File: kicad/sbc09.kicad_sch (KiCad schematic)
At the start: 78 parts, among them J1 Conn_01x04_Male, J2 Conn_01x06_Male, J3 Conn_01x06_Male, J4 Conn_01x06_Male, J5 Conn_02x05_Odd_Even, J6 Conn_02x25_Odd_Even, J7 Conn_02x05_Odd_Even, Q1 2N7000, SW1 SW_Push, U1 74HCT245, U10 SST39SF040-DIP, U11 XR68C681CJ, U12 MAX232, U2 74HCT245, U3 74HCT245, U4 MC6809E, U5 74HCT32, U6 EPM7128SLC84, U7 71256SA15TPG, U8 AS6C4008-55PCN, U9 SST39SF040-DIP, X1 8MHz, X2 3.6864MHz

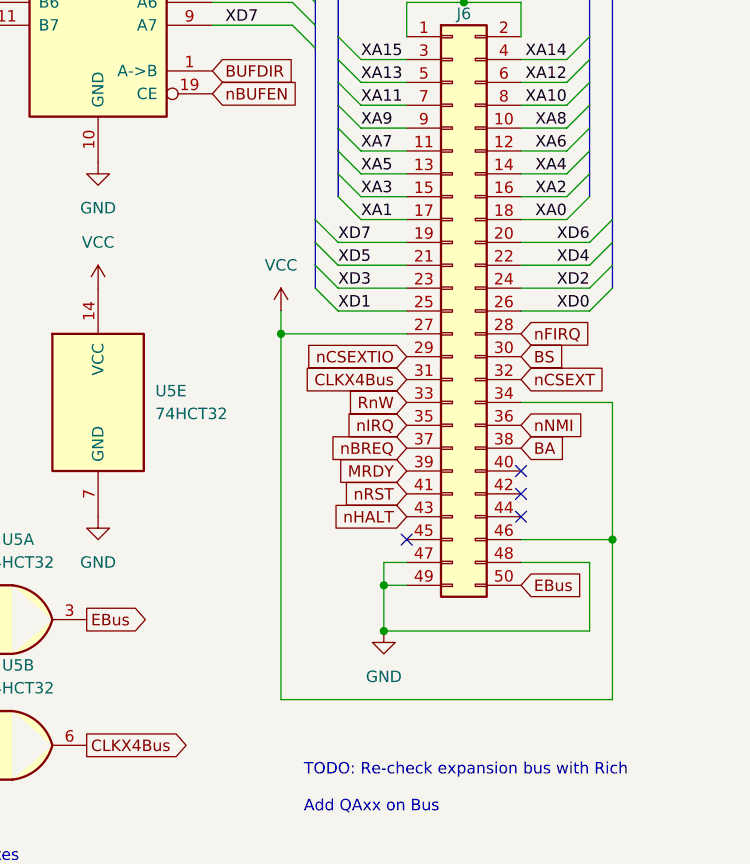
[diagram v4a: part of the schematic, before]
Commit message: KiCAD: Split VCC/VCCBUS and redraw planes
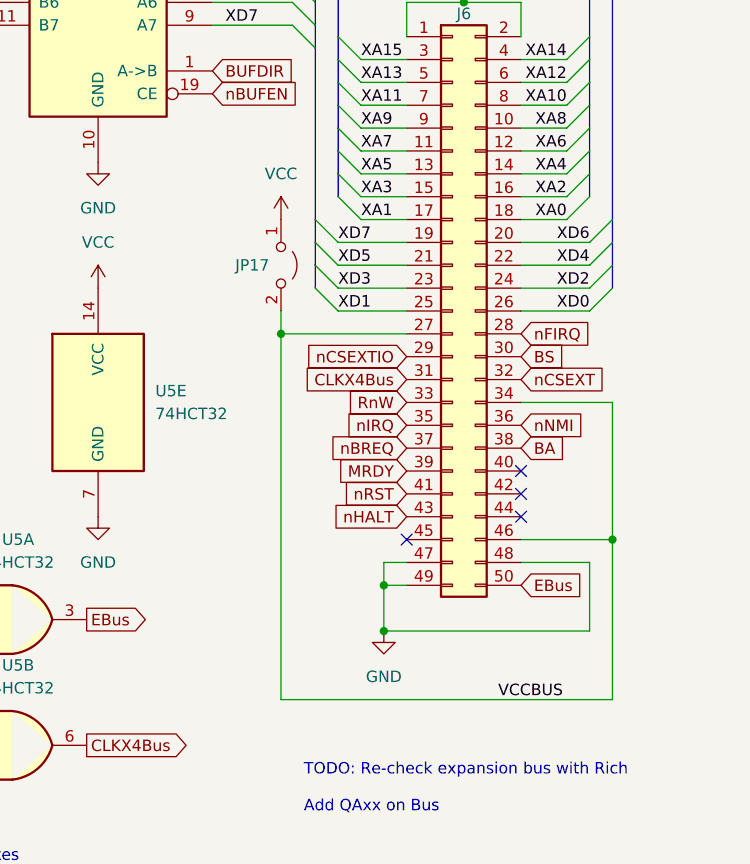
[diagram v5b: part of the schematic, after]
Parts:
- added JP17: Jumper_2_Open, Connector_PinHeader_2.54mm:PinHeader_1x02_P2.54mm_Vertical, symbol Jumper:Jumper_2_Open
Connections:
- net VCC: now also JP17.1 (A); no longer J6.27 (Pin_27), J6.34 (Pin_34), J6.46 (Pin_46)
- new net VCCBUS: J6.27 (Pin_27), J6.34 (Pin_34), J6.46 (Pin_46), JP17.2 (B)
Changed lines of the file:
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@@
     (effects (font (size 1.27 1.27)) (justify left bottom))
   )
+  (label "VCCBUS" (at 387.35 237.49 0)
+    (effects (font (size 1.27 1.27)) (justify left bottom))
+  )
   (label "XD4" (at 360.68 154.94 180)
     (effects (font (size 1.27 1.27)) (justify right bottom))
@@
     (pin "1")
   )
+  (symbol (lib_id "Jumper:Jumper_2_Open") (at 363.22 189.23 270) (unit 1)
+    (in_bom yes) (on_board yes)
+    (property "Reference" "JP17" (id 0) (at 358.14 189.23 90)
+      (effects (font (size 1.27 1.27)) (justify left))
+    )
+    (property "Value" "Jumper_2_Open" (id 1) (at 367.03 189.23 0)
+      (effects (font (size 1.27 1.27)) hide)
+    )
+    (property "Footprint" "Connector_PinHeader_2.54mm:PinHeader_1x02_P2.54mm_Vertical" (id 2) (at 363.22 189.23 0)
+      (effects (font (size 1.27 1.27)) hide)
+    )
+    (property "Datasheet" "~" (id 3) (at 363.22 189.23 0)
+      (effects (font (size 1.27 1.27)) hide)
+    )
+    (pin "1")
+    (pin "2")
+  )
   (symbol (lib_id "Device:C") (at 56.388 228.346 0) (unit 1)
     (in_bom yes) (on_board yes) (fields_autoplaced)
@@
     (pin "9")
   )
-  (symbol (lib_id "power:VCC") (at 363.22 194.31 0) (unit 1)
+  (symbol (lib_id "power:VCC") (at 363.22 184.15 0) (unit 1)
     (in_bom yes) (on_board yes) (fields_autoplaced)
-    (property "Reference" "#PWR061" (id 0) (at 363.22 198.12 0)
+    (property "Reference" "#PWR061" (id 0) (at 363.22 187.96 0)
       (effects (font (size 1.27 1.27)) hide)
     )
-    (property "Value" "VCC" (id 1) (at 363.22 189.23 0))
-    (property "Footprint" "" (id 2) (at 363.22 194.31 0)
+    (property "Value" "VCC" (id 1) (at 363.22 179.07 0))
+    (property "Footprint" "" (id 2) (at 363.22 184.15 0)
       (effects (font (size 1.27 1.27)) hide)
     )
-    (property "Datasheet" "" (id 3) (at 363.22 194.31 0)
+    (property "Datasheet" "" (id 3) (at 363.22 184.15 0)
       (effects (font (size 1.27 1.27)) hide)
     )
@@
       (reference "JP16") (unit 1) (value "Jumper_3_Bridged12") (footprint "Connector_PinHeader_2.54mm:PinHeader_1x03_P2.54mm_Vertical")
     )
+    (path "/3d764d21-3969-42e7-b769-dfffb0df0926"
+      (reference "JP17") (unit 1) (value "Jumper_2_Open") (footprint "Connector_PinHeader_2.54mm:PinHeader_1x02_P2.54mm_Vertical")
+    )
     (path "/262aa419-0fa8-4016-95e2-b1df66d01220"

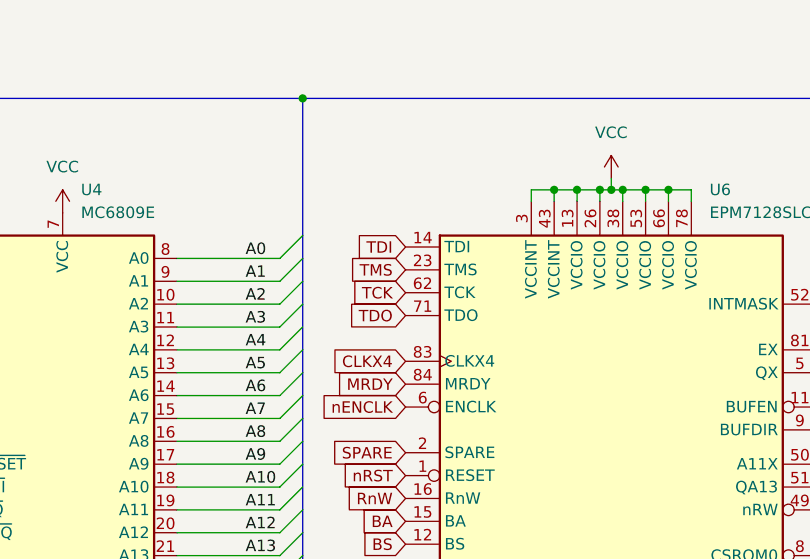
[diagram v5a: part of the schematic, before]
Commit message: KiCAD: Add jumper inline with CPLD pin 84 for 12V injection
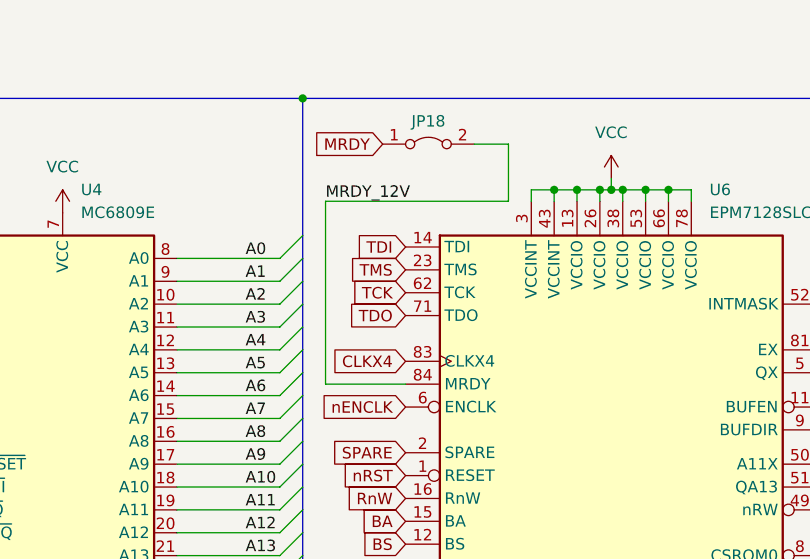
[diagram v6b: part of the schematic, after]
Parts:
- added JP18: Jumper_2_Bridged, Connector_PinHeader_2.54mm:PinHeader_1x02_P2.54mm_Vertical, symbol Jumper:Jumper_2_Bridged
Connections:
- net MRDY: now also JP18.1 (A); no longer U6.84 (MRDY)
- new net MRDY_12V: JP18.2 (B), U6.84 (MRDY)
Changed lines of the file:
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@@
     (stroke (width 0) (type default) (color 0 0 0 0))
   )
+  (wire (pts (xy 93.98 34.29) (xy 93.98 54.61))
+    (stroke (width 0) (type default) (color 0 0 0 0))
+  )
   (wire (pts (xy 24.13 71.12) (xy 24.13 97.79))
     (stroke (width 0) (type default) (color 0 0 0 0))
@@
     (stroke (width 0) (type default) (color 0 0 0 0))
   )
+  (wire (pts (xy 93.98 54.61) (xy 102.87 54.61))
+    (stroke (width 0) (type default) (color 0 0 0 0))
+  )
   (bus (pts (xy 201.93 86.36) (xy 201.93 88.9))
     (stroke (width 0) (type default) (color 0 0 0 0))
@@
     (stroke (width 0) (type default) (color 0 0 0 0))
   )
+  (wire (pts (xy 114.3 27.94) (xy 114.3 34.29))
+    (stroke (width 0) (type default) (color 0 0 0 0))
+  )
   (wire (pts (xy 166.37 124.46) (xy 167.64 124.46))
     (stroke (width 0) (type default) (color 0 0 0 0))
@@
     (stroke (width 0) (type default) (color 0 0 0 0))
   )
+  (wire (pts (xy 114.3 34.29) (xy 93.98 34.29))
+    (stroke (width 0) (type default) (color 0 0 0 0))
+  )
   (bus (pts (xy 304.8 48.26) (xy 304.8 50.8))
     (stroke (width 0) (type default) (color 0 0 0 0))
@@
     (stroke (width 0) (type default) (color 0 0 0 0))
   )
+  (wire (pts (xy 110.49 27.94) (xy 114.3 27.94))
+    (stroke (width 0) (type default) (color 0 0 0 0))
+  )
   (wire (pts (xy 259.08 78.74) (xy 259.08 111.76))
     (stroke (width 0) (type default) (color 0 0 0 0))
@@
     (effects (font (size 1.27 1.27)) (justify left bottom))
   )
+  (label "MRDY_12V" (at 93.98 34.29 0)
+    (effects (font (size 1.27 1.27)) (justify left bottom))
+  )
   (label "QA17" (at 154.94 116.84 180)
     (effects (font (size 1.27 1.27)) (justify right bottom))
@@
     )
   )
-  (global_label "MRDY" (shape input) (at 102.87 54.61 180) (fields_autoplaced)
+  (global_label "MRDY" (shape input) (at 100.33 27.94 180) (fields_autoplaced)
     (effects (font (size 1.27 1.27)) (justify right))
-    (property "Intersheet References" "${INTERSHEET_REFS}" (id 0) (at 95.3769 54.5306 0)
+    (property "Intersheet References" "${INTERSHEET_REFS}" (id 0) (at 92.8369 27.8606 0)
       (effects (font (size 1.27 1.27)) (justify right) hide)
     )
@@
     )
   )
+  (symbol (lib_id "Jumper:Jumper_2_Bridged") (at 105.41 27.94 0) (unit 1)
+    (in_bom yes) (on_board yes)
+    (property "Reference" "JP18" (id 0) (at 105.41 25.4 0))
+    (property "Value" "Jumper_2_Bridged" (id 1) (at 105.41 24.13 0)
+      (effects (font (size 1.27 1.27)) hide)
+    )
+    (property "Footprint" "Connector_PinHeader_2.54mm:PinHeader_1x02_P2.54mm_Vertical" (id 2) (at 105.41 27.94 0)
+      (effects (font (size 1.27 1.27)) hide)
+    )
+    (property "Datasheet" "~" (id 3) (at 105.41 27.94 0)
+      (effects (font (size 1.27 1.27)) hide)
+    )
+    (pin "1")
+    (pin "2")
+  )
   (symbol (lib_id "power:GND") (at 28.575 154.305 0) (unit 1)
     (in_bom yes) (on_board yes)
@@
       (reference "JP17") (unit 1) (value "Jumper_2_Open") (footprint "Connector_PinHeader_2.54mm:PinHeader_1x02_P2.54mm_Vertical")
     )
+    (path "/01c4ca08-8a4f-4fcc-ac99-649d9d9accf3"
+      (reference "JP18") (unit 1) (value "Jumper_2_Bridged") (footprint "Connector_PinHeader_2.54mm:PinHeader_1x02_P2.54mm_Vertical")
+    )
     (path "/262aa419-0fa8-4016-95e2-b1df66d01220"

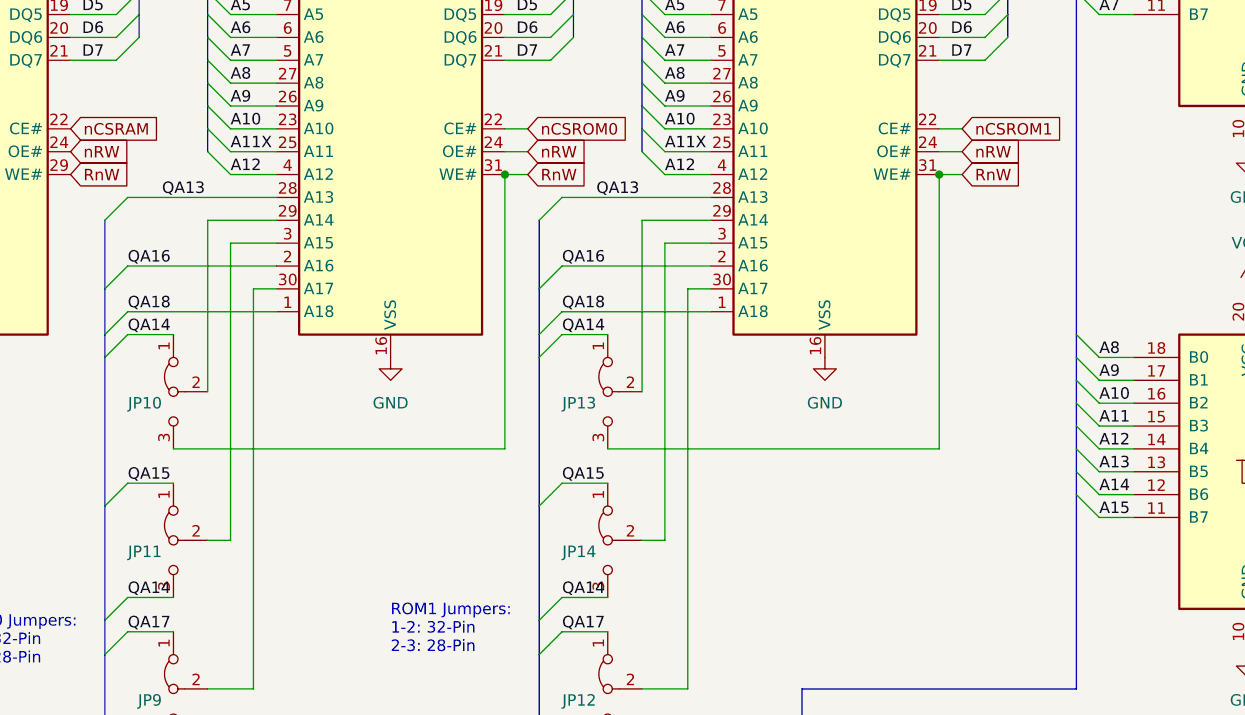
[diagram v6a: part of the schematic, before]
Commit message: KiCAD: Add jumper to isolate ROMs from RnW
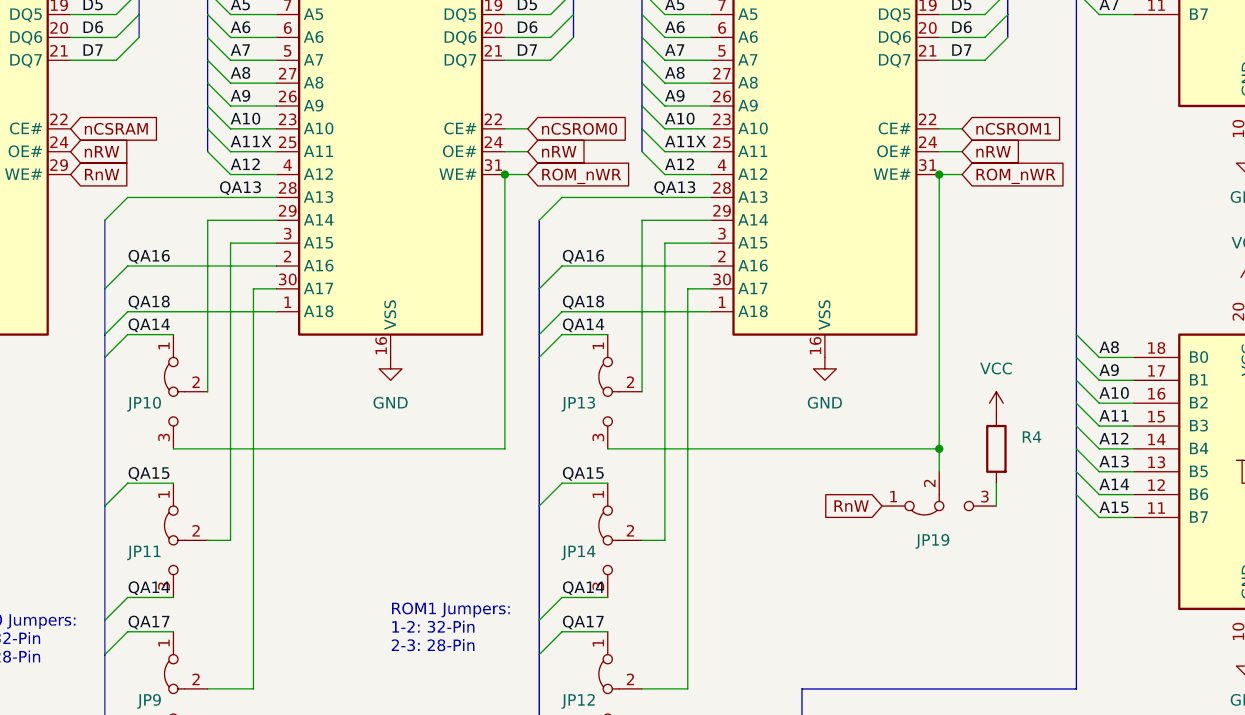
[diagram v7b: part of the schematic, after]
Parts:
- added JP19: Jumper_3_Bridged12, Connector_PinHeader_2.54mm:PinHeader_1x03_P2.54mm_Vertical, symbol Jumper:Jumper_3_Bridged12
- added R4: (no value), Resistor_THT:R_Axial_DIN0207_L6.3mm_D2.5mm_P10.16mm_Horizontal, symbol Device:R
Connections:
- net RnW: now also JP19.1 (A); no longer JP10.3 (B), JP13.3 (B), U10.31 (WE#), U9.31 (WE#)
- net VCC: now also R4.1
- new net: JP19.3 (B), R4.2
- new net ROM_nWR: JP10.3 (B), JP13.3 (B), JP19.2 (C), U10.31 (WE#), U9.31 (WE#)
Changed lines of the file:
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@@
   (junction (at 124.46 149.86) (diameter 0) (color 0 0 0 0)
   )
+  (junction (at 337.82 101.6) (diameter 0) (color 0 0 0 0)
+  )
   (junction (at 132.08 267.97) (diameter 0) (color 0 0 0 0)
   )
@@
     (stroke (width 0) (type default) (color 0 0 0 0))
   )
+  (wire (pts (xy 337.82 101.6) (xy 337.82 104.14))
+    (stroke (width 0) (type default) (color 0 0 0 0))
+  )
   (wire (pts (xy 17.78 53.34) (xy 26.67 53.34))
     (stroke (width 0) (type default) (color 0 0 0 0))
@@
     (stroke (width 0) (type default) (color 0 0 0 0))
   )
+  (wire (pts (xy 344.17 105.41) (xy 344.17 107.95))
+    (stroke (width 0) (type default) (color 0 0 0 0))
+  )
   (bus (pts (xy 391.16 104.14) (xy 391.16 106.68))
     (stroke (width 0) (type default) (color 0 0 0 0))
@@
     (effects (font (size 1.27 1.27)) (justify left bottom))
   )
-  (label "QA13" (at 251.46 73.66 0)
+  (label "QA13" (at 257.81 73.66 0)
     (effects (font (size 1.27 1.27)) (justify left bottom))
   )
@@
     (effects (font (size 1.27 1.27)) (justify left bottom))
   )
-  (label "QA13" (at 299.72 73.66 0)
+  (label "QA13" (at 306.07 73.66 0)
     (effects (font (size 1.27 1.27)) (justify left bottom))
   )
@@
     )
   )
+  (global_label "RnW" (shape input) (at 331.47 107.95 180) (fields_autoplaced)
+    (effects (font (size 1.27 1.27)) (justify right))
+    (property "Intersheet References" "${INTERSHEET_REFS}" (id 0) (at 325.1864 107.8706 0)
+      (effects (font (size 1.27 1.27)) (justify right) hide)
+    )
+  )
   (global_label "RnW" (shape input) (at 102.87 67.31 180) (fields_autoplaced)
     (effects (font (size 1.27 1.27)) (justify right))
@@
     )
   )
-  (global_label "RnW" (shape input) (at 340.36 71.12 0) (fields_autoplaced)
+  (global_label "ROM_nWR" (shape input) (at 340.36 71.12 0) (fields_autoplaced)
     (effects (font (size 1.27 1.27)) (justify left))
-    (property "Intersheet References" "${INTERSHEET_REFS}" (id 0) (at 346.6436 71.0406 0)
+    (property "Intersheet References" "${INTERSHEET_REFS}" (id 0) (at 351.6631 71.0406 0)
       (effects (font (size 1.27 1.27)) (justify left) hide)
     )
@@
     )
   )
+  (global_label "ROM_nWR" (shape input) (at 292.1 71.12 0) (fields_autoplaced)
+    (effects (font (size 1.27 1.27)) (justify left))
+    (property "Intersheet References" "${INTERSHEET_REFS}" (id 0) (at 303.4031 71.0406 0)
+      (effects (font (size 1.27 1.27)) (justify left) hide)
+    )
+  )
   (global_label "nHALT" (shape input) (at 377.19 217.17 180) (fields_autoplaced)
     (effects (font (size 1.27 1.27)) (justify right))
@@
     )
   )
-  (global_label "RnW" (shape input) (at 292.1 71.12 0) (fields_autoplaced)
-    (effects (font (size 1.27 1.27)) (justify left))
-    (property "Intersheet References" "${INTERSHEET_REFS}" (id 0) (at 298.3836 71.0406 0)
-      (effects (font (size 1.27 1.27)) (justify left) hide)
-    )
-  )
   (global_label "nRST" (shape input) (at 102.87 64.77 180) (fields_autoplaced)
     (effects (font (size 1.27 1.27)) (justify right))
@@
     (pin "1")
   )
+  (symbol (lib_id "power:VCC") (at 344.17 97.79 0) (unit 1)
+    (in_bom yes) (on_board yes)
+    (property "Reference" "#PWR08" (id 0) (at 344.17 101.6 0)
+      (effects (font (size 1.27 1.27)) hide)
+    )
+    (property "Value" "VCC" (id 1) (at 344.17 92.71 0))
+    (property "Footprint" "" (id 2) (at 344.17 97.79 0)
+      (effects (font (size 1.27 1.27)) hide)
+    )
+    (property "Datasheet" "" (id 3) (at 344.17 97.79 0)
+      (effects (font (size 1.27 1.27)) hide)
+    )
+    (pin "1")
+  )
   (symbol (lib_id "74xx:74LS245") (at 372.11 104.14 0) (mirror y) (unit 1)
     (in_bom yes) (on_board yes) (fields_autoplaced)
@@
     (pin "1")
   )
+  (symbol (lib_id "Jumper:Jumper_3_Bridged12") (at 337.82 107.95 0) (mirror x) (unit 1)
+    (in_bom yes) (on_board yes)
+    (property "Reference" "JP19" (id 0) (at 335.28 111.76 0)
+      (effects (font (size 1.27 1.27)) (justify left))
+    )
+    (property "Value" "Jumper_3_Bridged12" (id 1) (at 336.5501 110.49 90)
+      (effects (font (size 1.27 1.27)) (justify left) hide)
+    )
+    (property "Footprint" "Connector_PinHeader_2.54mm:PinHeader_1x03_P2.54mm_Vertical" (id 2) (at 337.82 107.95 0)
+      (effects (font (size 1.27 1.27)) hide)
+    )
+    (property "Datasheet" "~" (id 3) (at 337.82 107.95 0)
+      (effects (font (size 1.27 1.27)) hide)
+    )
+    (pin "1")
+    (pin "2")
+    (pin "3")
+  )
   (symbol (lib_id "Device:C") (at 50.165 269.494 0) (unit 1)
     (in_bom yes) (on_board yes) (fields_autoplaced)
@@
     (pin "2")
   )
+  (symbol (lib_id "Device:R") (at 344.17 101.6 0) (mirror y) (unit 1)
+    (in_bom yes) (on_board yes)
+    (property "Reference" "R4" (id 0) (at 349.25 100.33 0)
+      (effects (font (size 1.27 1.27)) (justify left))
+    )
+    (property "Value" "" (id 1) (at 350.52 102.87 0)
+      (effects (font (size 1.27 1.27)) (justify left))
+    )
+    (property "Footprint" "Resistor_THT:R_Axial_DIN0207_L6.3mm_D2.5mm_P10.16mm_Horizontal" (id 2) (at 345.948 101.6 90)
+      (effects (font (size 1.27 1.27)) hide)
+    )
+    (property "Datasheet" "~" (id 3) (at 344.17 101.6 0)
+      (effects (font (size 1.27 1.27)) hide)
+    )
+    (pin "1")
+    (pin "2")
+  )
   (symbol (lib_id "power:GND") (at 180.34 132.08 0) (unit 1)
     (in_bom yes) (on_board yes)
@@
       (reference "#PWR07") (unit 1) (value "GND") (footprint "")
     )
+    (path "/8fa90343-1520-41e6-8a65-12896914bf58"
+      (reference "#PWR08") (unit 1) (value "VCC") (footprint "")
+    )
     (path "/d66abdc1-6b13-4c39-a8a9-fd74eb244498"
       (reference "#PWR010") (unit 1) (value "GND") (footprint "")
@@
       (reference "JP18") (unit 1) (value "Jumper_2_Bridged") (footprint "Connector_PinHeader_2.54mm:PinHeader_1x02_P2.54mm_Vertical")
     )
+    (path "/d0b423ae-0ca9-48d8-86d2-465b8e350aef"
+      (reference "JP19") (unit 1) (value "Jumper_3_Bridged12") (footprint "Connector_PinHeader_2.54mm:PinHeader_1x03_P2.54mm_Vertical")
+    )
     (path "/262aa419-0fa8-4016-95e2-b1df66d01220"
       (reference "Q1") (unit 1) (value "2N7000") (footprint "Package_TO_SOT_THT:TO-92_Inline")
@@
       (reference "R3") (unit 1) (value "470R") (footprint "Resistor_THT:R_Axial_DIN0207_L6.3mm_D2.5mm_P10.16mm_Horizontal")
     )
+    (path "/d2f8692f-7c3e-451c-af8e-9291ccc61146"
+      (reference "R4") (unit 1) (value "4K7") (footprint "Resistor_THT:R_Axial_DIN0207_L6.3mm_D2.5mm_P10.16mm_Horizontal")
+    )
     (path "/d942ef75-7728-43ee-ba65-19df17fecb1a"
